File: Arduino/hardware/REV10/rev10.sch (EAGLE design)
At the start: 26 parts, among them IC1 ATmega328P-PU, Q1 32768Hz, U1 TC1185SMD, U2 ARDUINOR3-DIMENSION

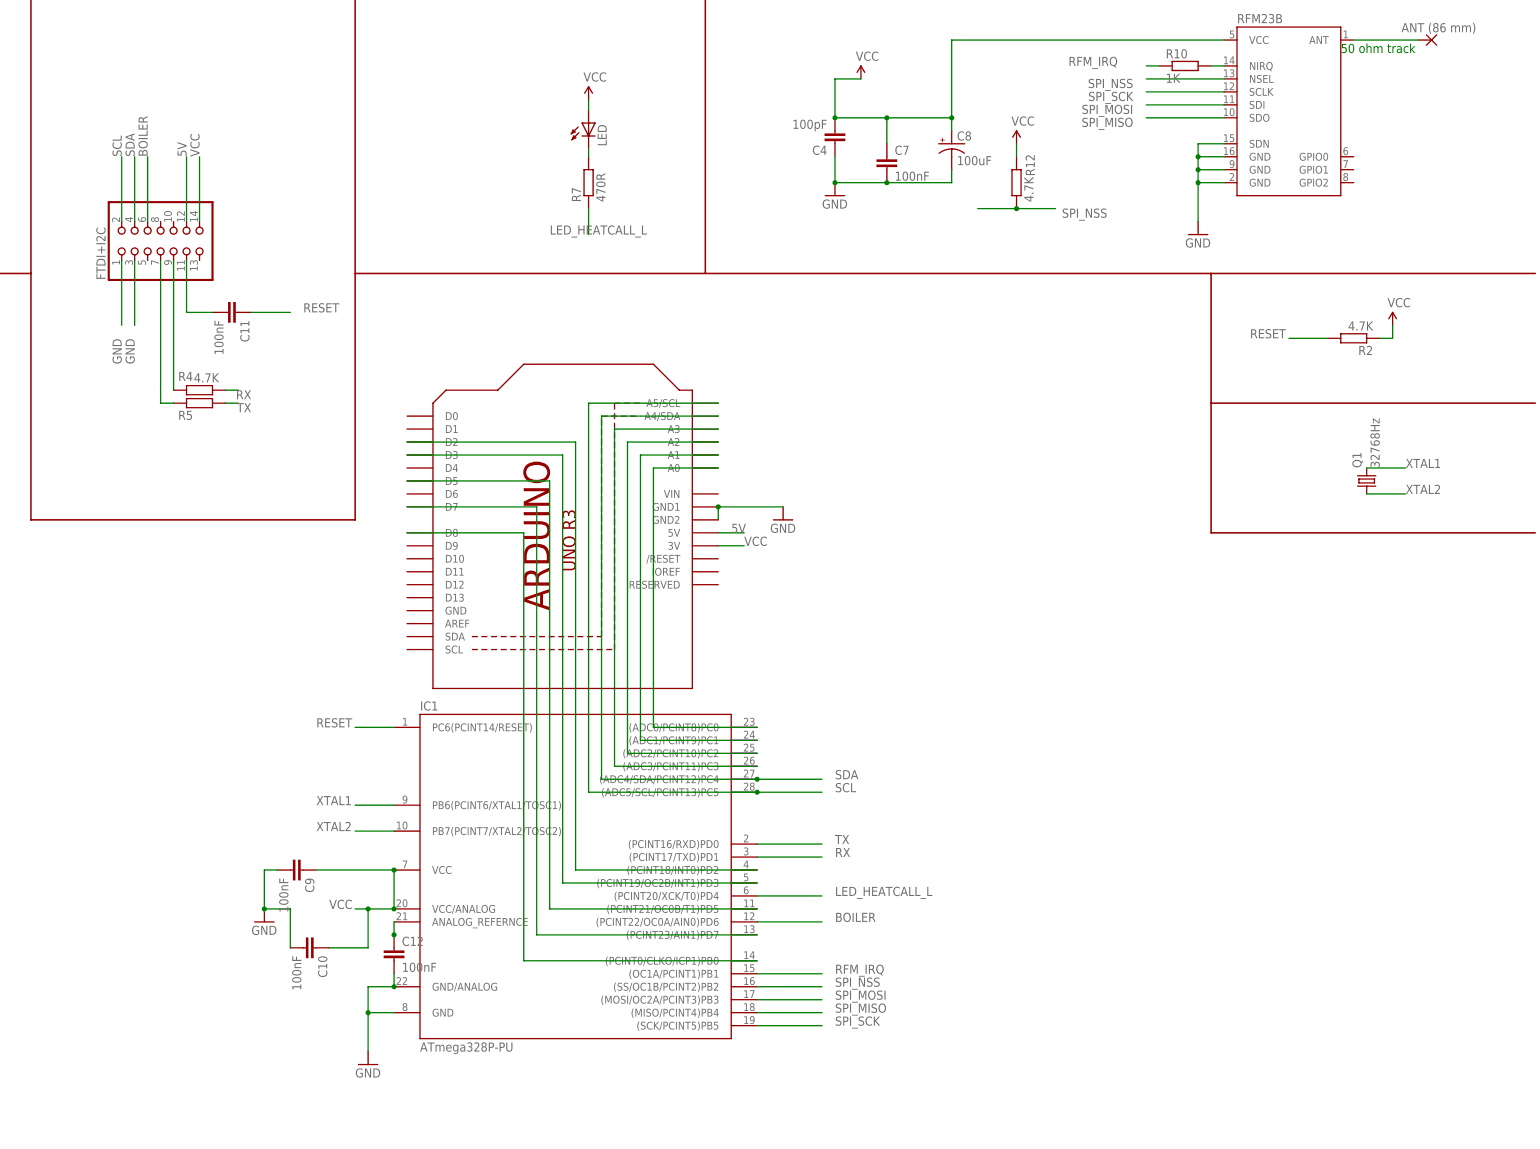
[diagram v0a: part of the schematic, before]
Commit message: updated rev10 to smd avr and placed i2c connector
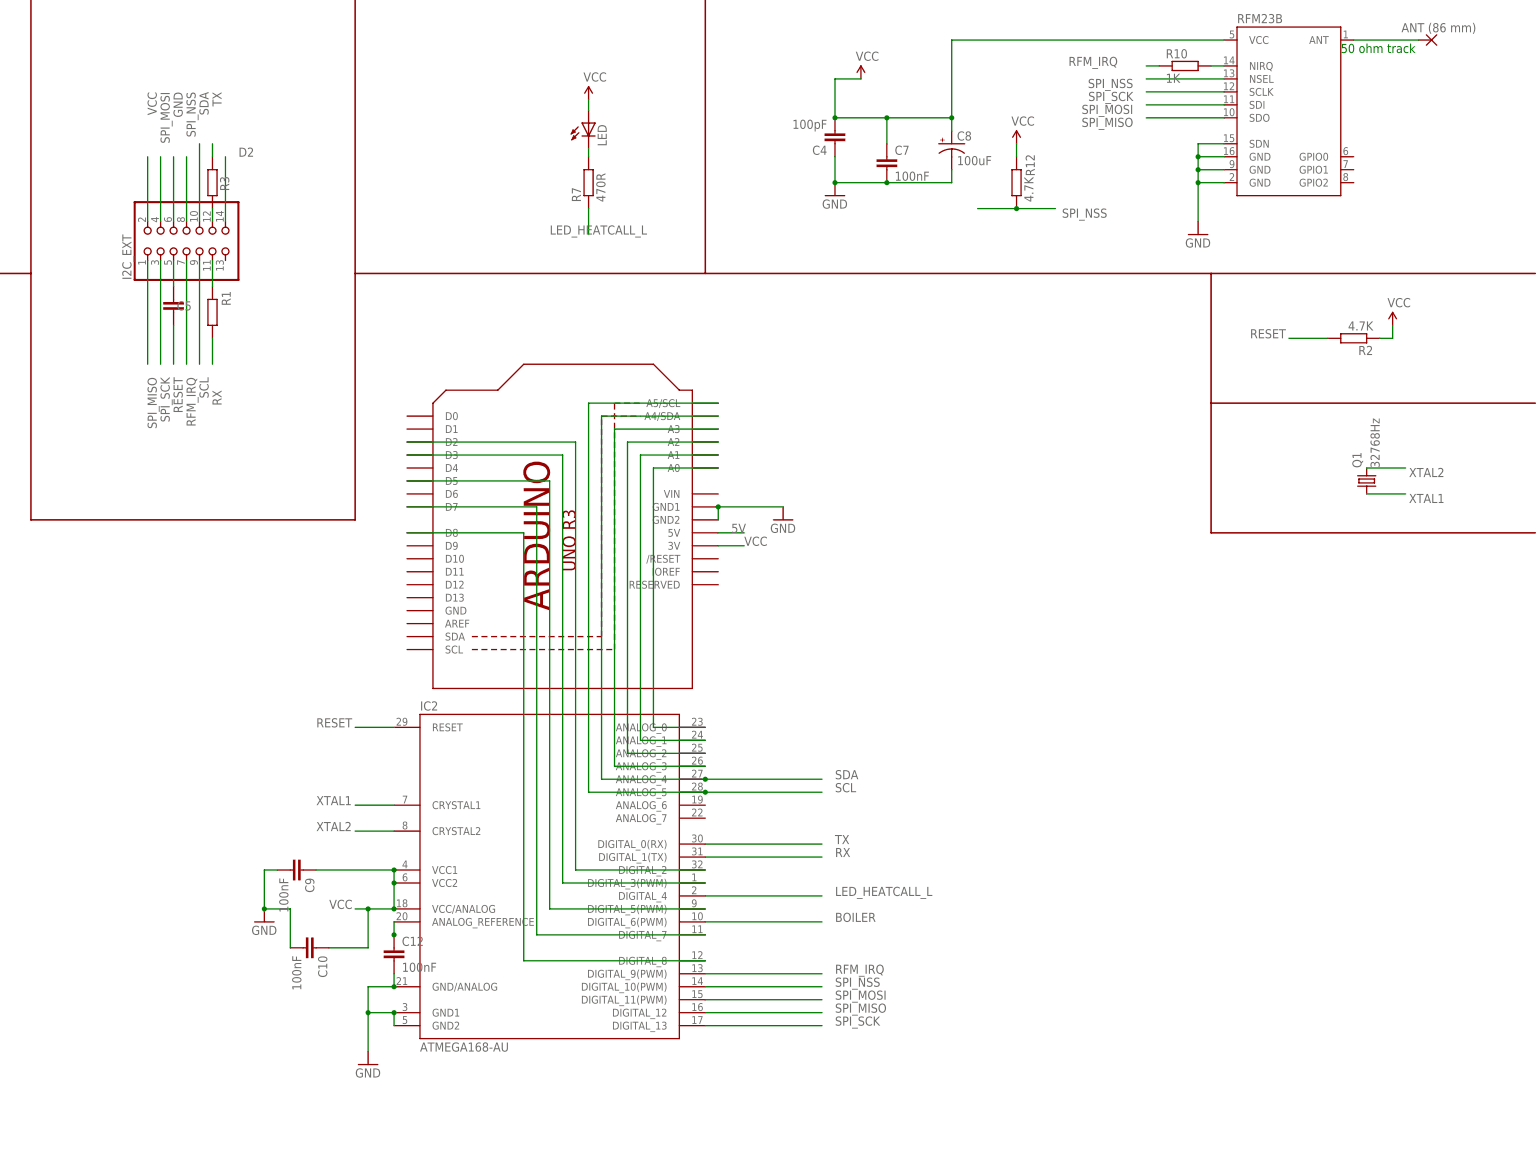
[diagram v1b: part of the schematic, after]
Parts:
- removed C11: 100nF, resistor:C-EUC0603
- removed FTDI+I2C: (no value), pinhead:PINHD-2X7
- removed IC1: ATmega328P-PU, Arduino-AVR:ATMEGA168-PU
- removed R4, R5: 4.7K, resistor:R-EU_R0603
- added C5: 100nF, resistor:C-EUC0603
- added I2C_EXT: (no value), pinhead:PINHD-2X7
- added IC2: ATMEGA168-AU, Arduino-AVR:ATMEGA168-AU
- added R1, R3: 4.7K, resistor:R-EU_R0603
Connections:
- removed net N$1: C11.2, FTDI+I2C.11
- removed net N$3: FTDI+I2C.7, R5.2
- removed net N$5: FTDI+I2C.9, R4.2
- new net D2: I2C_EXT.14
- new net N$25: C5.2, I2C_EXT.5
- new net N$26: I2C_EXT.12, R3.2
- new net N$28: I2C_EXT.11, R1.2
- net 5V: no longer FTDI+I2C.12
- net BOILER: now also IC2.DIGITAL_6(PWM); no longer FTDI+I2C.6, IC1.(PCINT22/OC0A/AIN0)PD6
- net GND: now also I2C_EXT.6, IC2.GND/ANALOG, IC2.GND1, IC2.GND2; no longer FTDI+I2C.1, FTDI+I2C.3, IC1.GND, IC1.GND/ANALOG
- net LED_HEATCALL_L: now also IC2.DIGITAL_4; no longer IC1.(PCINT20/XCK/T0)PD4
- net N$14: now also IC2.ANALOG_0; no longer IC1.(ADC0/PCINT8)PC0
- net N$15: now also IC2.ANALOG_1; no longer IC1.(ADC1/PCINT9)PC1
- net N$16: now also IC2.ANALOG_2; no longer IC1.(ADC2/PCINT10)PC2
- net N$17: now also IC2.ANALOG_3; no longer IC1.(ADC3/PCINT11)PC3
- net N$19: now also IC2.DIGITAL_8; no longer IC1.(PCINT0/CLKO/ICP1)PB0
- net N$20: now also IC2.DIGITAL_5(PWM); no longer IC1.(PCINT21/OC0B/T1)PD5
- net N$21: now also IC2.DIGITAL_7; no longer IC1.(PCINT23/AIN1)PD7
- net N$22: now also IC2.DIGITAL_2; no longer IC1.(PCINT18/INT0)PD2
- net N$24: now also IC2.DIGITAL_3(PWM); no longer IC1.(PCINT19/OC2B/INT1)PD3
- net N$6: now also IC2.ANALOG_REFERENCE; no longer IC1.ANALOG_REFERNCE
- net RESET: now also C5.1, IC2.RESET; no longer C11.1, IC1.PC6(PCINT14/RESET)
- net RFM_IRQ: now also I2C_EXT.7, IC2.DIGITAL_9(PWM); no longer IC1.(OC1A/PCINT1)PB1
- net RX: now also IC2.DIGITAL_1(TX), R1.1; no longer IC1.(PCINT17/TXD)PD1, R4.1
- net SCL: now also I2C_EXT.9, IC2.ANALOG_5; no longer FTDI+I2C.2, IC1.(ADC5/SCL/PCINT13)PC5
- net SDA: now also I2C_EXT.10, IC2.ANALOG_4; no longer FTDI+I2C.4, IC1.(ADC4/SDA/PCINT12)PC4
- net SPI_MISO: now also I2C_EXT.1, IC2.DIGITAL_12; no longer IC1.(MISO/PCINT4)PB4
- net SPI_MOSI: now also I2C_EXT.4, IC2.DIGITAL_11(PWM); no longer IC1.(MOSI/OC2A/PCINT3)PB3
- net SPI_NSS: now also I2C_EXT.8, IC2.DIGITAL_10(PWM); no longer IC1.(SS/OC1B/PCINT2)PB2
- net SPI_SCK: now also I2C_EXT.3, IC2.DIGITAL_13; no longer IC1.(SCK/PCINT5)PB5
- net TX: now also IC2.DIGITAL_0(RX), R3.1; no longer IC1.(PCINT16/RXD)PD0, R5.1
- net VCC: now also I2C_EXT.2, IC2.VCC/ANALOG, IC2.VCC1, IC2.VCC2; no longer FTDI+I2C.14, IC1.VCC, IC1.VCC/ANALOG
- net XTAL1: now also IC2.CRYSTAL1, Q1.1; no longer IC1.PB6(PCINT6/XTAL1/TOSC1), Q1.2
- net XTAL2: now also IC2.CRYSTAL2, Q1.2; no longer IC1.PB7(PCINT7/XTAL2/TOSC2), Q1.1

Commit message: updates to rev10 as per deniz spec
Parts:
- added R4: 4.7K, resistor:R-EU_R0603
- added R5: 330R, resistor:R-EU_R0603
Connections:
- new net N$1: IC2.DIGITAL_7, R4.1
- new net N$3: IC2.DIGITAL_8, R5.1
- net N$19: now also R5.2; no longer IC2.DIGITAL_8
- net N$21: now also R4.2; no longer IC2.DIGITAL_7
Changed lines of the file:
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@@
 <?xml version="1.0" encoding="utf-8"?>
 <!DOCTYPE eagle SYSTEM "eagle.dtd">
-<eagle version="7.3.0">
+<eagle version="7.4.0">
 <drawing>
 <settings>
@@
 <part name="I2C_EXT" library="pinhead" deviceset="PINHD-2X7" device=""/>
 <part name="IC2" library="Arduino-AVR" deviceset="ATMEGA168" device="-AU"/>
+<part name="R4" library="resistor" deviceset="R-EU_" device="R0603" value="4.7K"/>
+<part name="R5" library="resistor" deviceset="R-EU_" device="R0603" value="330R"/>
 </parts>
 <sheets>
@@
 <instance part="I2C_EXT" gate="A" x="124.46" y="213.36" rot="R90"/>
 <instance part="IC2" gate="1" x="195.58" y="91.44"/>
+<instance part="R4" gate="G$1" x="198.12" y="78.74" smashed="yes" rot="R180">
+<attribute name="NAME" x="196.85" y="82.3214" size="1.778" layer="95" rot="R180"/>
+</instance>
+<instance part="R5" gate="G$1" x="200.66" y="73.66" smashed="yes" rot="R180">
+<attribute name="NAME" x="199.39" y="77.2414" size="1.778" layer="95" rot="R180"/>
+</instance>
 </instances>
 <busses>
@@
 <net name="N$21" class="0">
 <segment>
-<wire x1="226.06" y1="78.74" x2="193.04" y2="78.74" width="0.1524" layer="91"/>
 <wire x1="193.04" y1="78.74" x2="193.04" y2="162.56" width="0.1524" layer="91"/>
 <wire x1="193.04" y1="162.56" x2="167.64" y2="162.56" width="0.1524" layer="91"/>
-<pinref part="IC2" gate="1" pin="DIGITAL_7"/>
+<pinref part="R4" gate="G$1" pin="2"/>
 </segment>
 </net>
 <net name="N$19" class="0">
 <segment>
-<wire x1="226.06" y1="73.66" x2="190.5" y2="73.66" width="0.1524" layer="91"/>
 <wire x1="190.5" y1="73.66" x2="190.5" y2="157.48" width="0.1524" layer="91"/>
 <pinref part="U2" gate="G$1" pin="D8"/>
 <wire x1="190.5" y1="157.48" x2="167.64" y2="157.48" width="0.1524" layer="91"/>
-<pinref part="IC2" gate="1" pin="DIGITAL_8"/>
+<pinref part="R5" gate="G$1" pin="2"/>
+<wire x1="195.58" y1="73.66" x2="190.5" y2="73.66" width="0.1524" layer="91"/>
 </segment>
 </net>
@@
 </segment>
 </net>
+<net name="N$1" class="0">
+<segment>
+<pinref part="R4" gate="G$1" pin="1"/>
+<pinref part="IC2" gate="1" pin="DIGITAL_7"/>
+<wire x1="203.2" y1="78.74" x2="226.06" y2="78.74" width="0.1524" layer="91"/>
+</segment>
+</net>
+<net name="N$3" class="0">
+<segment>
+<pinref part="R5" gate="G$1" pin="1"/>
+<pinref part="IC2" gate="1" pin="DIGITAL_8"/>
+<wire x1="205.74" y1="73.66" x2="226.06" y2="73.66" width="0.1524" layer="91"/>
+</segment>
+</net>

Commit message: updates as pr google doc
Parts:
- removed C3: 10uF 10V, resistor:C-EUC0603
- removed U$3: TUHS10, tuhs10:TUHS10
- added A6, A7: WIREPAD1,6/0,9, wirepad:WIREPAD1,6/0,9
- added LDR: BPX65, opto-trans-siemens:BPX65
- added R6: 100K, resistor:R-EU_R0603
- added R8: 4K7, resistor:R-EU_R0603
- added R9: 4.7K, resistor:R-EU_R0603
- added TMP112: TMP1, TMP112_2:TMP112
- added U$4: VTX-214-010-205, VTX-214-010-205:VTX-214-010-205
- added USBPOWER: MICRO-USB-FCI-10103592, micro-usb-fci-10103592:MICRO-USB-FCI-10103592
- I2C_EXT: device pinhead:PINHD-2X7 -> pinhead:PINHD-2X7/90
- R4: value 4.7K -> 4K7
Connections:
- removed net N$11: C3.1, U$3.BC-
- removed net N$12: C3.2, U$3.BC+
- removed net N$14: IC2.ANALOG_0, U2.A0
- removed net N$21: R4.2
- removed net N$22: IC2.DIGITAL_2, U2.D2
- new net 5V1: USBPOWER.VCC
- new net IO_POWER_UP: IC2.DIGITAL_7, LDR.C
- new net LDR: IC2.ANALOG_0, LDR.A, R6.1
- new net N$5: A7.P, IC2.ANALOG_7
- net 5V: no longer U$3.+
- net D2: now also IC2.DIGITAL_2, R9.1
- net GND: now also R6.2, TMP112.ADD0, TMP112.GND, USBPOWER.GND, USBPOWER.SHIELD@5, USBPOWER.SHIELD@8; no longer U$3.-
- net N$1: now also A6.P, IC2.ANALOG_6; no longer IC2.DIGITAL_7, R4.1
- net N$4: no longer U$3.AC2
- net N$8: now also U$4.L; no longer U$3.AC1
- net SCL: now also R8.1, TMP112.SCL
- net SDA: now also R4.2, TMP112.SDA
- net VCC: now also R4.1, R8.2, R9.2, TMP112.V+
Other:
- moved on the sheet: R4

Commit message: updates as pr google doc and guidance from mark and deniz
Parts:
- removed A6, A7: WIREPAD1,6/0,9, wirepad:WIREPAD1,6/0,9
- added JP1: (no value), pinhead:PINHD-2X4/90
- added LED1: (no value), adafruit:LED3MM
- added R11: 470R, resistor:R-EU_R0603
- added R13: 1K, resistor:R-EU_R0603
- added R14: 10K, resistor:R-EU_R0603
- added T1: (no value), transistor:-NPN-SOT23-EBC
- added X2: (no value), con-wago-500:W237-102
- renumbered LDR to PHT, U$4 to PSU
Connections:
- removed net N$17: IC2.ANALOG_3, U2.A3
- removed net N$24: IC2.DIGITAL_3(PWM), U2.D3
- new net N$11: IC2.ANALOG_2
- new net N$12: R13.2, R14.2, T1.B
- new net N$14: LED1.C, T1.C, X2-1.KL
- new net VOICE: IC2.DIGITAL_3(PWM)
- net 5V: now also R11.2, X2-2.KL
- net BOILER: now also R13.1
- net GND: now also JP1.5, R14.1, T1.E, U2.GND
- net N$1: now also JP1.1; no longer A6.P
- net N$16: now also LED1.A, R11.1; no longer IC2.ANALOG_2, U2.A2
- net N$19: no longer U2.D8
- net N$20: no longer U2.D5
- net N$5: now also JP1.3; no longer A7.P
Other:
- note added: "On BOM"

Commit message: minor changes to board
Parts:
- removed JP1: (no value), pinhead:PINHD-2X4/90
- added JP2: (no value), pinhead:PINHD-2X3/90
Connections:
- net 5V: now also JP2.4, PSU.+
- net GND: now also JP2.5, PSU.-; no longer JP1.5
- net N$1: now also JP2.1; no longer JP1.1
- net N$4: now also PSU.N
- net N$5: now also JP2.3; no longer JP1.3
- net VCC: now also JP2.6
- net VOICE: now also JP2.2
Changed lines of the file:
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@@
 <part name="P+4" library="SparkFun-Aesthetics" deviceset="VCC" device=""/>
 <part name="PSU" library="VTX-214-010-205" deviceset="VTX-214-010-205" device=""/>
-<part name="JP1" library="pinhead" deviceset="PINHD-2X4" device="/90"/>
 <part name="GND6" library="SparkFun-Aesthetics" deviceset="GND" device=""/>
 <part name="GND9" library="SparkFun-Aesthetics" deviceset="GND" device=""/>
@@
 <part name="GND10" library="SparkFun-Aesthetics" deviceset="GND" device=""/>
 <part name="X2" library="con-wago-500" deviceset="W237-102" device=""/>
+<part name="JP2" library="pinhead" deviceset="PINHD-2X3" device="/90"/>
 </parts>
 <sheets>
@@
 <instance part="P+4" gate="1" x="58.42" y="106.68" rot="R180"/>
 <instance part="PSU" gate="G$1" x="40.64" y="185.42"/>
-<instance part="JP1" gate="A" x="276.86" y="104.14"/>
 <instance part="GND6" gate="1" x="269.24" y="101.6"/>
 <instance part="GND9" gate="1" x="157.48" y="139.7"/>
@@
 <instance part="X2" gate="-1" x="373.38" y="142.24" rot="R180"/>
 <instance part="X2" gate="-2" x="373.38" y="149.86" rot="R180"/>
+<instance part="JP2" gate="A" x="276.86" y="106.68"/>
 </instances>
 <busses>
@@
 </segment>
 <segment>
-<wire x1="274.32" y1="101.6" x2="274.32" y2="91.44" width="0.1524" layer="91"/>
-<label x="274.32" y="91.44" size="1.778" layer="95" rot="R90"/>
+<wire x1="281.94" y1="104.14" x2="292.1" y2="104.14" width="0.1524" layer="91"/>
+<label x="297.18" y="104.14" size="1.778" layer="95" rot="R180"/>
+<pinref part="JP2" gate="A" pin="6"/>
 </segment>
 </net>
@@
 <pinref part="GND1" gate="1" pin="GND"/>
 <wire x1="63.5" y1="180.34" x2="53.34" y2="180.34" width="0.1524" layer="91"/>
+<pinref part="PSU" gate="G$1" pin="-"/>
 </segment>
 <segment>
@@
 </segment>
 <segment>
-<pinref part="JP1" gate="A" pin="5"/>
 <pinref part="GND6" gate="1" pin="GND"/>
 <wire x1="269.24" y1="104.14" x2="274.32" y2="104.14" width="0.1524" layer="91"/>
+<pinref part="JP2" gate="A" pin="5"/>
 </segment>
 <segment>
@@
 <wire x1="53.34" y1="190.5" x2="63.5" y2="190.5" width="0.1524" layer="91"/>
 <label x="66.04" y="190.5" size="1.778" layer="95"/>
+<pinref part="PSU" gate="G$1" pin="+"/>
 </segment>
 <segment>
@@
 </segment>
 <segment>
-<wire x1="292.1" y1="101.6" x2="281.94" y2="101.6" width="0.1524" layer="91"/>
-<label x="292.1" y="101.6" size="1.778" layer="95"/>
+<wire x1="292.1" y1="106.68" x2="281.94" y2="106.68" width="0.1524" layer="91"/>
+<label x="294.64" y="106.68" size="1.778" layer="95"/>
+<pinref part="JP2" gate="A" pin="4"/>
 </segment>
 <segment>
@@
 <wire x1="25.4" y1="185.42" x2="25.4" y2="180.34" width="0.1524" layer="91"/>
 <wire x1="25.4" y1="180.34" x2="27.94" y2="180.34" width="0.1524" layer="91"/>
+<pinref part="PSU" gate="G$1" pin="N"/>
 </segment>
 </net>
@@
 <wire x1="261.62" y1="109.22" x2="261.62" y2="104.14" width="0.1524" layer="91"/>
 <wire x1="261.62" y1="104.14" x2="226.06" y2="104.14" width="0.1524" layer="91"/>
-<pinref part="JP1" gate="A" pin="1"/>
+<pinref part="JP2" gate="A" pin="1"/>
 </segment>
 </net>
@@
 <wire x1="264.16" y1="106.68" x2="264.16" y2="101.6" width="0.1524" layer="91"/>
 <wire x1="264.16" y1="101.6" x2="226.06" y2="101.6" width="0.1524" layer="91"/>
-<pinref part="JP1" gate="A" pin="3"/>
+<pinref part="JP2" gate="A" pin="3"/>
 </segment>
 </net>
@@
 </segment>
 <segment>
-<wire x1="299.72" y1="104.14" x2="281.94" y2="104.14" width="0.1524" layer="91"/>
-<label x="302.26" y="104.14" size="1.778" layer="95"/>
-</segment>
-</net>
+<wire x1="299.72" y1="109.22" x2="281.94" y2="109.22" width="0.1524" layer="91"/>
+<label x="299.72" y="109.22" size="1.778" layer="95"/>
+<pinref part="JP2" gate="A" pin="2"/>
+</segment>
+</net>

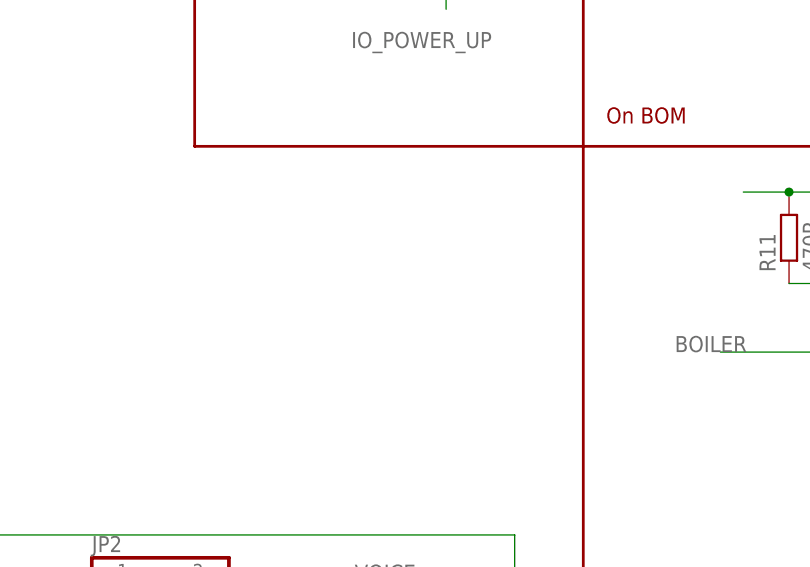
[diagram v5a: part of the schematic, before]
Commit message: pfet placed
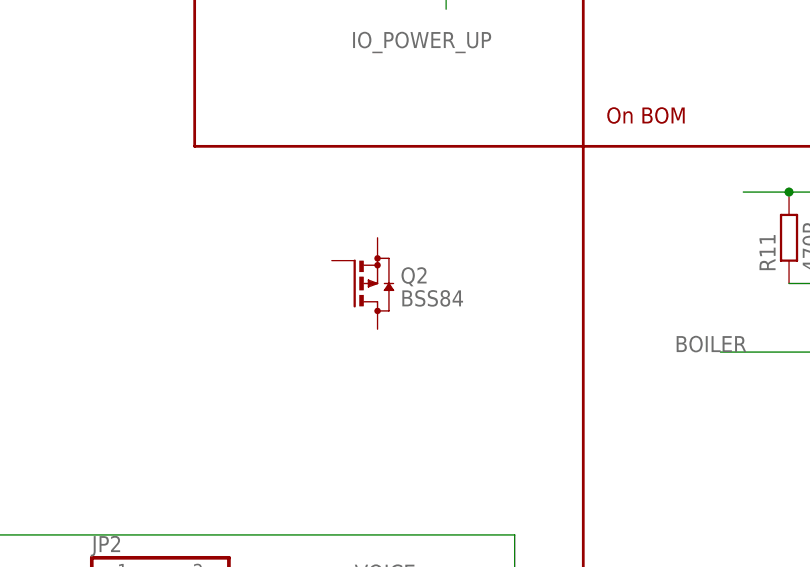
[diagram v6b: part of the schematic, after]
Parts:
- added Q2: BSS84, transistor-small-signal:BSS84
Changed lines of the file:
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@@
 <part name="X2" library="con-wago-500" deviceset="W237-102" device=""/>
 <part name="JP2" library="pinhead" deviceset="PINHD-2X3" device="/90"/>
+<part name="Q2" library="transistor-small-signal" deviceset="BSS84" device=""/>
 </parts>
 <sheets>
@@
 <instance part="X2" gate="-2" x="373.38" y="149.86" rot="R180"/>
 <instance part="JP2" gate="A" x="276.86" y="106.68"/>
+<instance part="Q2" gate="G$1" x="302.26" y="142.24"/>
 </instances>
 <busses>
